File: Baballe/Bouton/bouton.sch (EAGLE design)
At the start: 12 parts, among them IC1 74AHC1G04DBV, Q1 IRF7319

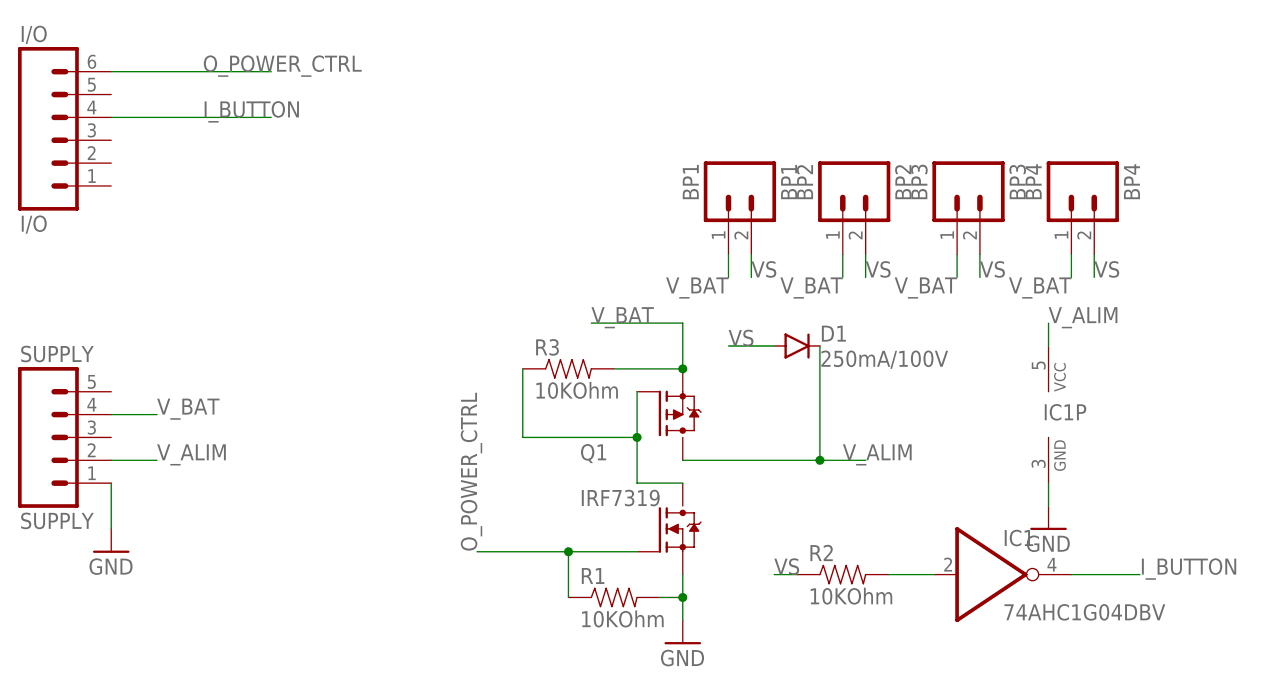
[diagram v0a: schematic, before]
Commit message: Correction des cartes alim et boutons suite à une erreur détectée lors de l'impression
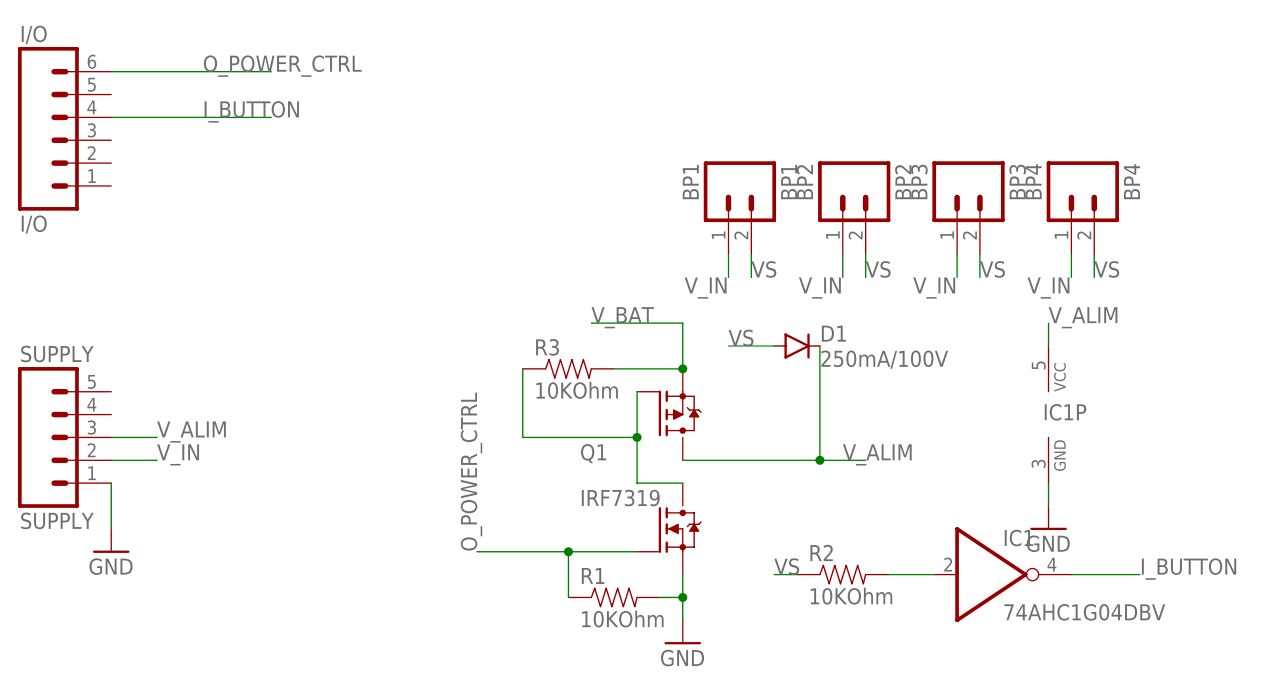
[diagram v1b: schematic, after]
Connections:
- new net V_IN: BP1.1, BP2.1, BP3.1, BP4.1, SUPPLY.2
- net V_ALIM: now also SUPPLY.3; no longer SUPPLY.2
- net V_BAT: no longer BP1.1, BP2.1, BP3.1, BP4.1, SUPPLY.4
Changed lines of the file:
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@@
 <net name="V_BAT" class="2">
-<segment>
-<wire x1="-63.5" y1="27.94" x2="-58.42" y2="27.94" width="0.1524" layer="91"/>
-<label x="-58.42" y="27.94" size="1.778" layer="95"/>
-<pinref part="SUPPLY" gate="G$1" pin="4"/>
-</segment>
-<segment>
-<pinref part="BP1" gate="G$1" pin="1"/>
-<wire x1="5.08" y1="45.72" x2="5.08" y2="43.18" width="0.1524" layer="91"/>
-<label x="5.08" y="43.18" size="1.778" layer="95" rot="R180"/>
-</segment>
-<segment>
-<pinref part="BP2" gate="G$1" pin="1"/>
-<wire x1="17.78" y1="45.72" x2="17.78" y2="43.18" width="0.1524" layer="91"/>
-<label x="17.78" y="43.18" size="1.778" layer="95" rot="R180"/>
-</segment>
-<segment>
-<pinref part="BP3" gate="G$1" pin="1"/>
-<wire x1="30.48" y1="45.72" x2="30.48" y2="43.18" width="0.1524" layer="91"/>
-<label x="30.48" y="43.18" size="1.778" layer="95" rot="R180"/>
-</segment>
-<segment>
-<pinref part="BP4" gate="G$1" pin="1"/>
-<wire x1="43.18" y1="45.72" x2="43.18" y2="43.18" width="0.1524" layer="91"/>
-<label x="43.18" y="43.18" size="1.778" layer="95" rot="R180"/>
-</segment>
 <segment>
 <pinref part="R3" gate="G$1" pin="2"/>
@@
 </net>
 <net name="V_ALIM" class="2">
-<segment>
-<pinref part="SUPPLY" gate="G$1" pin="2"/>
-<wire x1="-63.5" y1="22.86" x2="-58.42" y2="22.86" width="0.1524" layer="91"/>
-<label x="-58.42" y="22.86" size="1.778" layer="95"/>
-</segment>
 <segment>
 <pinref part="Q1" gate="G$1" pin="P-D"/>
@@
 <wire x1="40.64" y1="35.56" x2="40.64" y2="38.1" width="0.1524" layer="91"/>
 <label x="40.64" y="38.1" size="1.778" layer="95"/>
+</segment>
+<segment>
+<pinref part="SUPPLY" gate="G$1" pin="3"/>
+<wire x1="-63.5" y1="25.4" x2="-58.42" y2="25.4" width="0.1524" layer="91"/>
+<label x="-58.42" y="25.4" size="1.778" layer="95"/>
 </segment>
 </net>
@@
 </segment>
 </net>
+<net name="V_IN" class="2">
+<segment>
+<pinref part="BP1" gate="G$1" pin="1"/>
+<wire x1="5.08" y1="45.72" x2="5.08" y2="43.18" width="0.1524" layer="91"/>
+<label x="5.08" y="43.18" size="1.778" layer="95" rot="R180"/>
+</segment>
+<segment>
+<pinref part="BP2" gate="G$1" pin="1"/>
+<wire x1="17.78" y1="45.72" x2="17.78" y2="43.18" width="0.1524" layer="91"/>
+<label x="17.78" y="43.18" size="1.778" layer="95" rot="R180"/>
+</segment>
+<segment>
+<pinref part="BP3" gate="G$1" pin="1"/>
+<wire x1="30.48" y1="45.72" x2="30.48" y2="43.18" width="0.1524" layer="91"/>
+<label x="30.48" y="43.18" size="1.778" layer="95" rot="R180"/>
+</segment>
+<segment>
+<pinref part="BP4" gate="G$1" pin="1"/>
+<wire x1="43.18" y1="45.72" x2="43.18" y2="43.18" width="0.1524" layer="91"/>
+<label x="43.18" y="43.18" size="1.778" layer="95" rot="R180"/>
+</segment>
+<segment>
+<pinref part="SUPPLY" gate="G$1" pin="2"/>
+<wire x1="-63.5" y1="22.86" x2="-58.42" y2="22.86" width="0.1524" layer="91"/>
+<label x="-58.42" y="22.86" size="1.778" layer="95"/>
+</segment>
+</net>
